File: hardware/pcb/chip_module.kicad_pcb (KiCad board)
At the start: 6 copper layers, 150 x 140 mm, 201 parts, among them J12 BTB_DAUGHTER

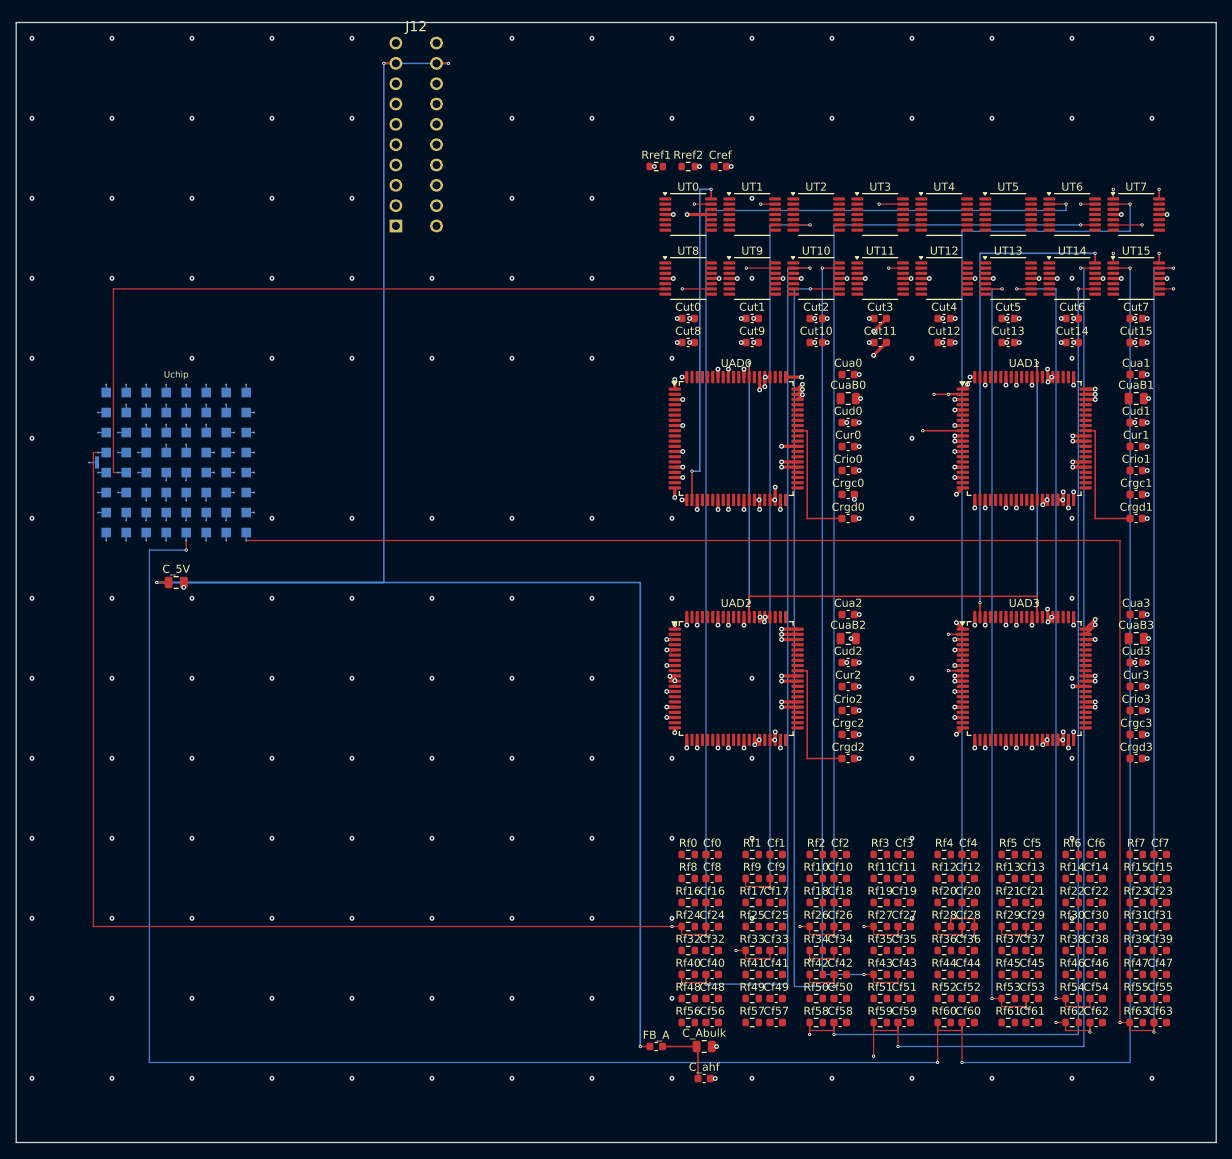
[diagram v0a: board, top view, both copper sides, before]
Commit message: pins: per-datasheet fixes (ADF4351 VCOM, FT232 CBUS0/NC, AP2127K pin4) + FPGA clock on P-side MRCC
Per-datasheet verification of all 11 components (real PDFs / KiCad symbols /
manufacturer datasheets) found 4 confirmed pin defects, now fixed:

- ADF4351 pin 23 (VCOM, internal compensation node biased at half the tuning
  range) was tied direct to GND -- shorting the half-range bias. Now decoupled
  to GND via a 100nF cap on a dedicated ADF_VCOM net (mirrors VREF/C36 and
  TEMP/C37). Verified from ADF4351.pdf p8 Pin Function table.
- FT232RL pin 23 is CBUS0 (not AGND); pin 24 is NC (not a 2nd VCC pad). The
  prior 'fix' tied 23->GND and 24->+3V3 under a wrong pin belief. Now both are
  no_connect; the real AGND is pin 25 (already GND). TXD/RXD comment labels
  corrected (nets are named from the FPGA side); 3V3OUT decoupler is C55 not C57.
  Verified from the KiCad Interface_USB:FT232RL symbol (omits NC pads 8 & 24).
- AP2127K-1.0 (REG3) fixed-output pin 4 is NC, not BP -- the prior C41 10nF
  tied a cap to a floating NC pad. Pin 4 -> no_connect; C41 designator reused
  for the ADF4351 VCOM decoupling cap. Noise reduction is via CIN/COUT
  (C42/C43/C44). Verified from Diodes AP2127K DS36478.
- FPGA clk_100mhz was on the N-side MRCC (A8), forcing a CLOCK_DEDICATED_ROUTE
  FALSE workaround (fabric routing, higher jitter). gen_fpga_ballmap_csg324.py
  now puts the input clock on the P-side MRCC (B8, dedicated delay-compensated
  route) and refclk_out on the N-side (A8); the XDC workaround is removed.
  Per UG472. Stale 'A14' doc references for refclk_25m corrected.

Label: the Abracon ASE 100 MHz oscillator is an XO (not a TCXO); schematic/BOM
value and comments corrected. Boards regenerated (both boards pick up the
ballmap swap + shared symbol-lib changes). HARDWARE_DESIGN.md pin-audit table
rows for FT232RL and ADF4351 corrected.

Co-Authored-By: Claude Code <noreply@anthropic.com>
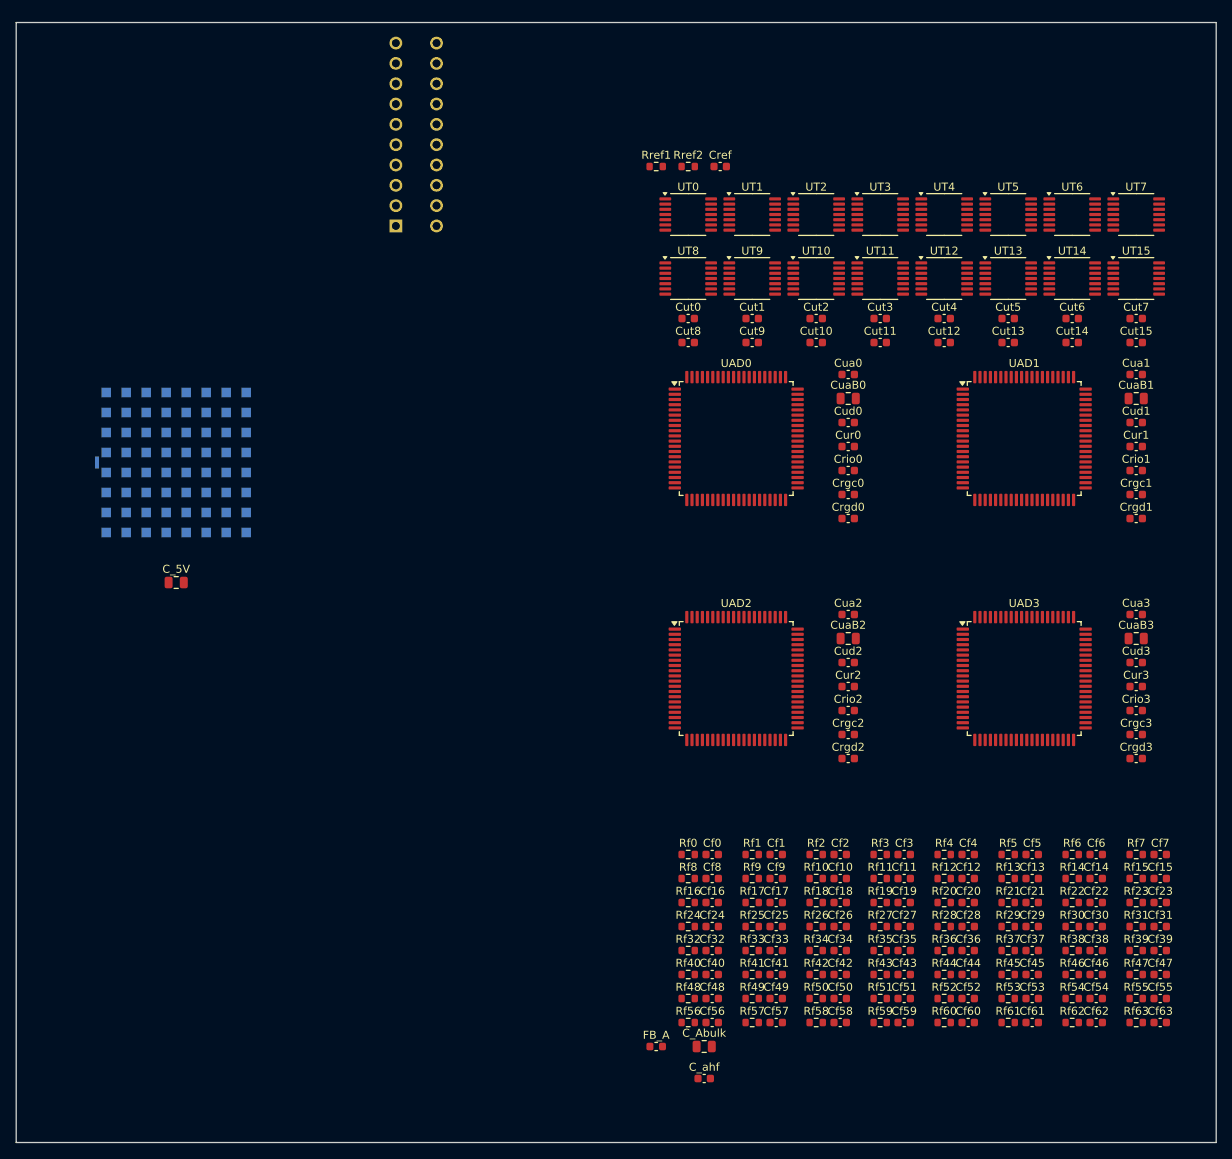
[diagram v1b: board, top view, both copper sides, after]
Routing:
- net DET_IN60: track 306.8 -> 0.00 mm, vias 5 -> 0
- net DET_IN59: track 288.9 -> 0.00 mm, vias 4 -> 0
- net DET_IN58: track 279.6 -> 0.00 mm, vias 4 -> 0
- net DET_IN24: track 279.2 -> 0.00 mm, vias 4 -> 0
- net DET_IN63: track 277.7 -> 0.00 mm, vias 4 -> 0
- net DET_IN62: track 277.6 -> 0.00 mm, vias 4 -> 0
- net DET_IN27: track 273.3 -> 0.00 mm, vias 4 -> 0
- net DET_IN26: track 272.0 -> 0.00 mm, vias 4 -> 0
- net DET_IN53: track 263.9 -> 0.00 mm, vias 4 -> 0
- net DET_IN34: track 248.3 -> 0.00 mm, vias 3 -> 0
- net DET_IN40: track 247.4 -> 0.00 mm, vias 4 -> 0
- net DET_IN33: track 236.8 -> 0.00 mm, vias 2 -> 0
- net +5V: track 225.5 -> 0.00 mm, vias 4 -> 0
- net GND: track 184.6 -> 0.00 mm, vias 336 -> 0
- net DET_TIA28: track 131.8 -> 0.00 mm, vias 4 -> 0
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- removed copper zone on In2.Cu, net +3V3
- removed copper zone on In1.Cu, net GND

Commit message: pcb(head): route_signals die-bus escape fanout (517 dog-bone vias) + planes
Head board at the pre-FreeRouting baseline: 64 detector electrodes + 64 TIA
inputs escaped with 2.5mm dog-bone vias clear of the 0.30mm field, planes
poured, DRC 0/0/0 (unconnected_items=ignore). Signal routing (via->TIA,
TIA->ADC, ADC->BTB J12) pending FreeRouting cycles — connectivity audit
shows 150 split / 79 dangling non-plane nets, all FreeRouting's remaining
job. Committed as a durable restore point before the autoroute cycles.

Co-Authored-By: Claude Code <noreply@anthropic.com>
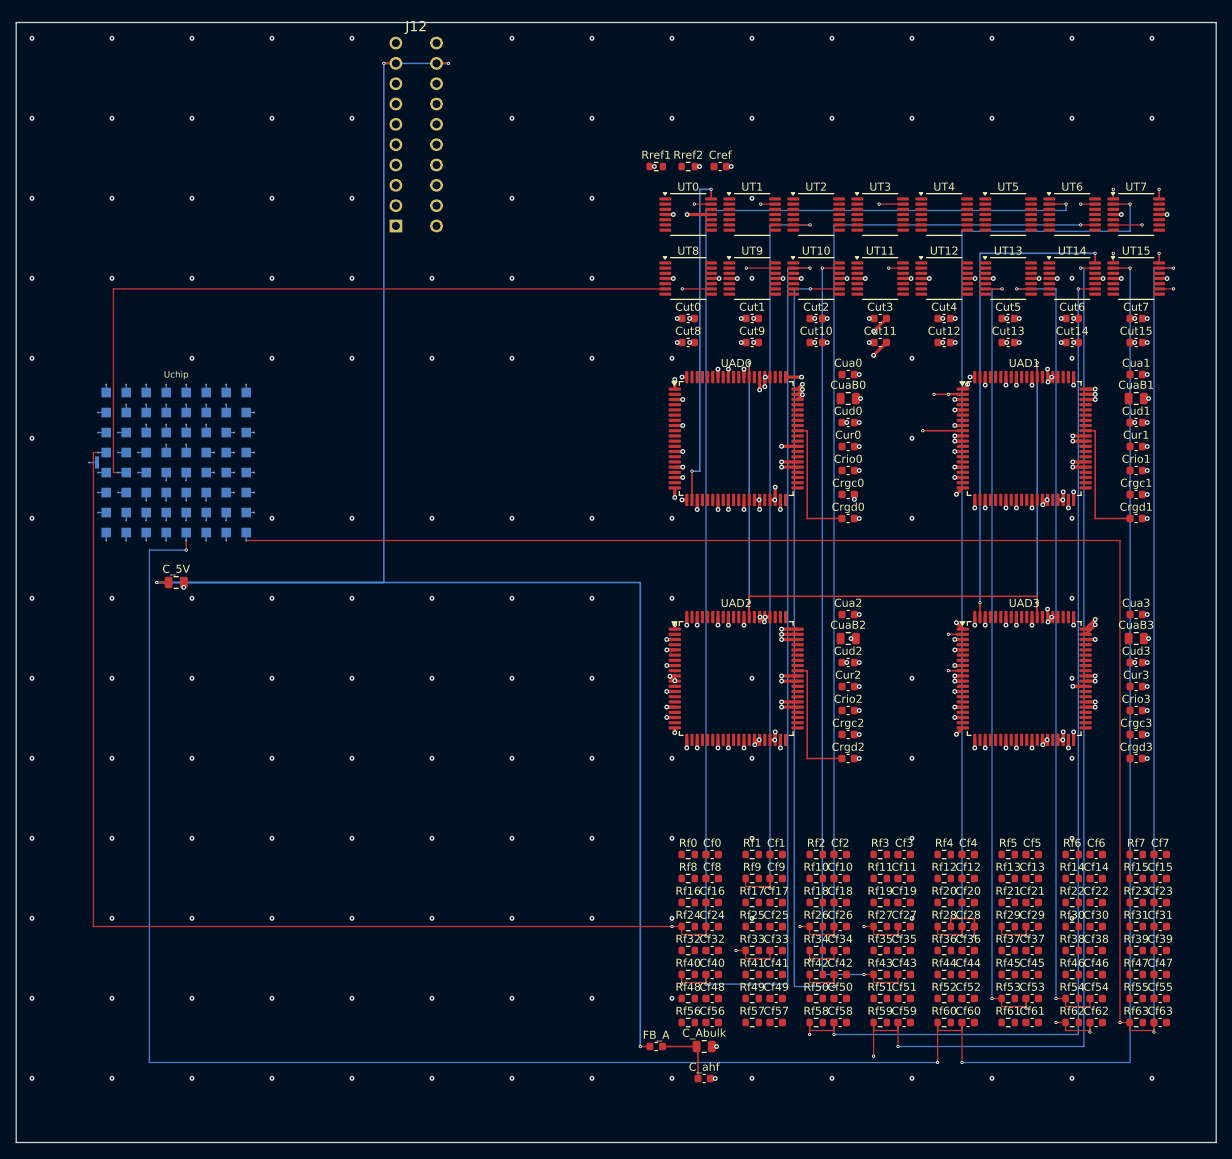
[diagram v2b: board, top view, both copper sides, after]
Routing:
- net DET_IN60: track 0.00 -> 306.8 mm, vias 0 -> 5
- net DET_IN59: track 0.00 -> 288.9 mm, vias 0 -> 4
- net DET_IN58: track 0.00 -> 279.6 mm, vias 0 -> 4
- net DET_IN24: track 0.00 -> 279.2 mm, vias 0 -> 4
- net DET_IN63: track 0.00 -> 277.7 mm, vias 0 -> 4
- net DET_IN62: track 0.00 -> 277.6 mm, vias 0 -> 4
- net DET_IN27: track 0.00 -> 273.3 mm, vias 0 -> 4
- net DET_IN26: track 0.00 -> 272.0 mm, vias 0 -> 4
- net DET_IN53: track 0.00 -> 263.9 mm, vias 0 -> 4
- net DET_IN34: track 0.00 -> 248.3 mm, vias 0 -> 3
- net DET_IN40: track 0.00 -> 247.4 mm, vias 0 -> 4
- net DET_IN33: track 0.00 -> 236.8 mm, vias 0 -> 2
- net +5V: track 0.00 -> 225.5 mm, vias 0 -> 4
- net GND: track 0.00 -> 184.6 mm, vias 0 -> 336
- net DET_TIA28: track 0.00 -> 131.8 mm, vias 0 -> 4
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- added copper zone on In2.Cu, net +3V3
- added copper zone on In1.Cu, net GND
